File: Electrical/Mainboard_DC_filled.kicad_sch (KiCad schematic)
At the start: 42 parts, among them J1 Serial Connector, Q1 TIP41C, Q2 TIP41C, U1 L7805CV, U2 Teensy3.5, U3 L7805CV, U4 6N137, U5 6N137, U6 6N137, U7 6N137

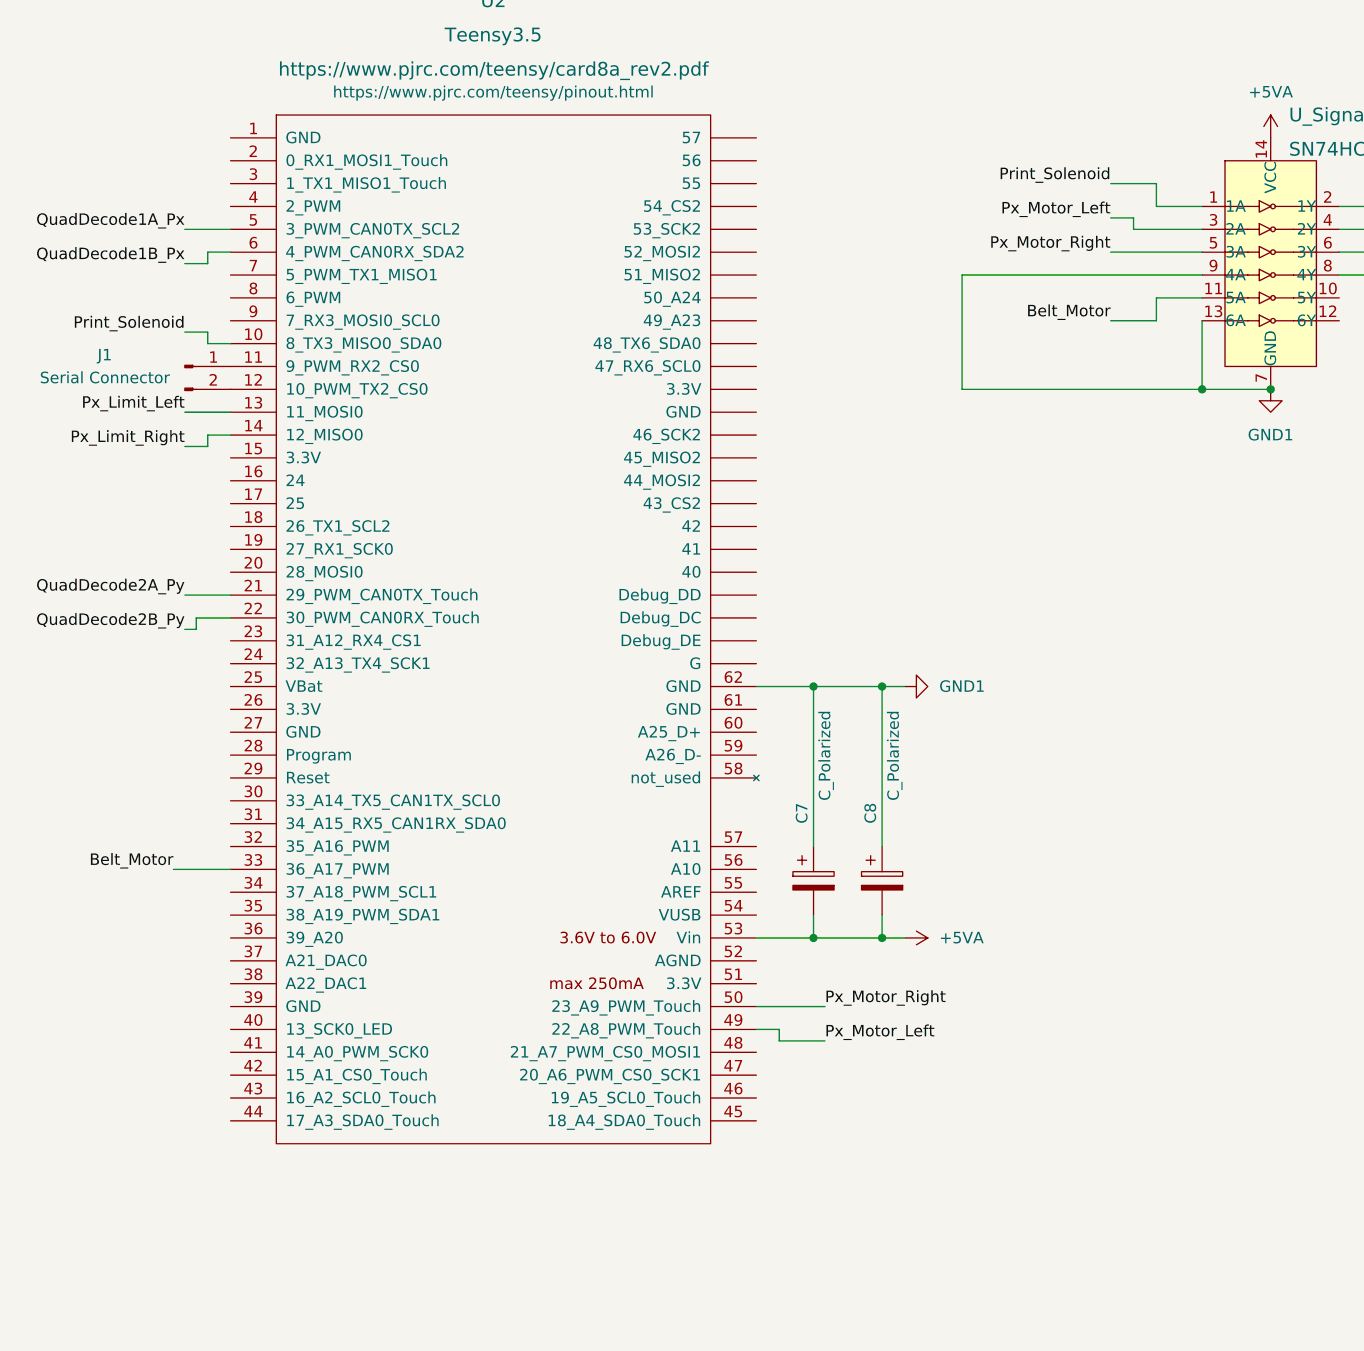
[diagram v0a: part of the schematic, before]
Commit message: Fixed PCB Error
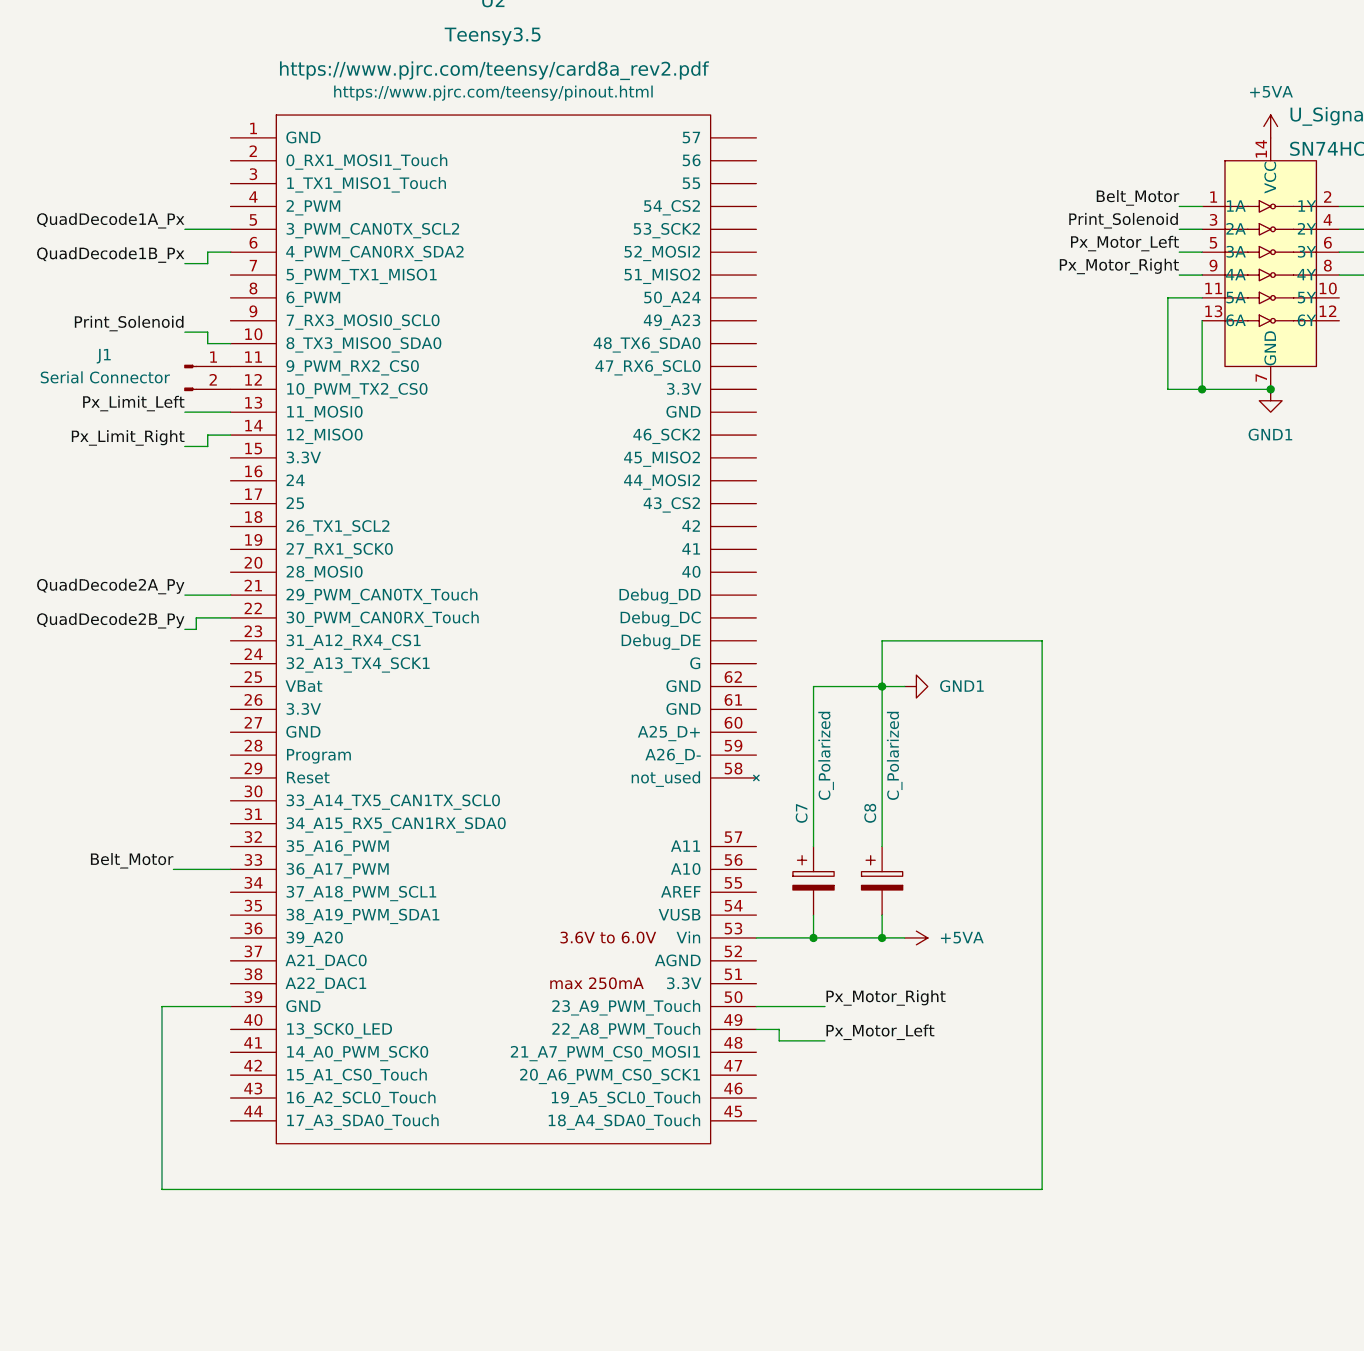
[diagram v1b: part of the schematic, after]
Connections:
- net Belt_Motor: now also U_Signal_Output1.1 (1A); no longer U_Signal_Output1.11 (5A)
- net GND1: now also U2.39 (GND), U_Signal_Output1.11 (5A); no longer U2.62 (GND), U_Signal_Output1.9 (4A)
- net Print_Solenoid: now also U_Signal_Output1.3 (2A); no longer U_Signal_Output1.1 (1A)
- net Px_Motor_Left: now also U_Signal_Output1.5 (3A); no longer U_Signal_Output1.3 (2A)
- net Px_Motor_Right: now also U_Signal_Output1.9 (4A); no longer U_Signal_Output1.5 (3A)
